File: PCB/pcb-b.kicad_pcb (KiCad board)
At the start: 2 copper layers, 117.6 x 56.4 mm, 90 parts, among them Q1 BC817, Q10 BC817, Q11 TPCA8120,L1Q, Q12 BC817, Q13 TPCA8120,L1Q, Q14 BC817, Q15 BC817, Q17 BC327, Q18 BC327, Q19 BC817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

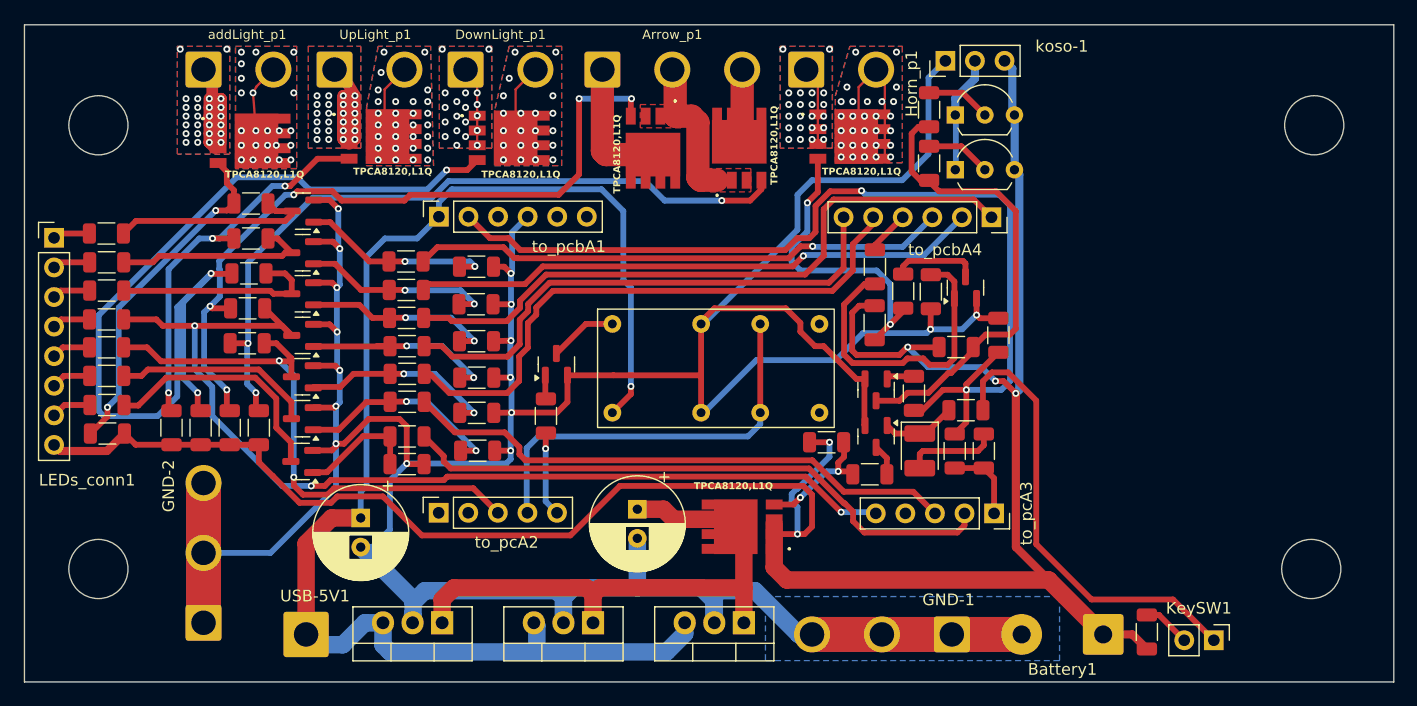
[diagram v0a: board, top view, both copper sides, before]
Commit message: Mechanic relay substitution and size reducing
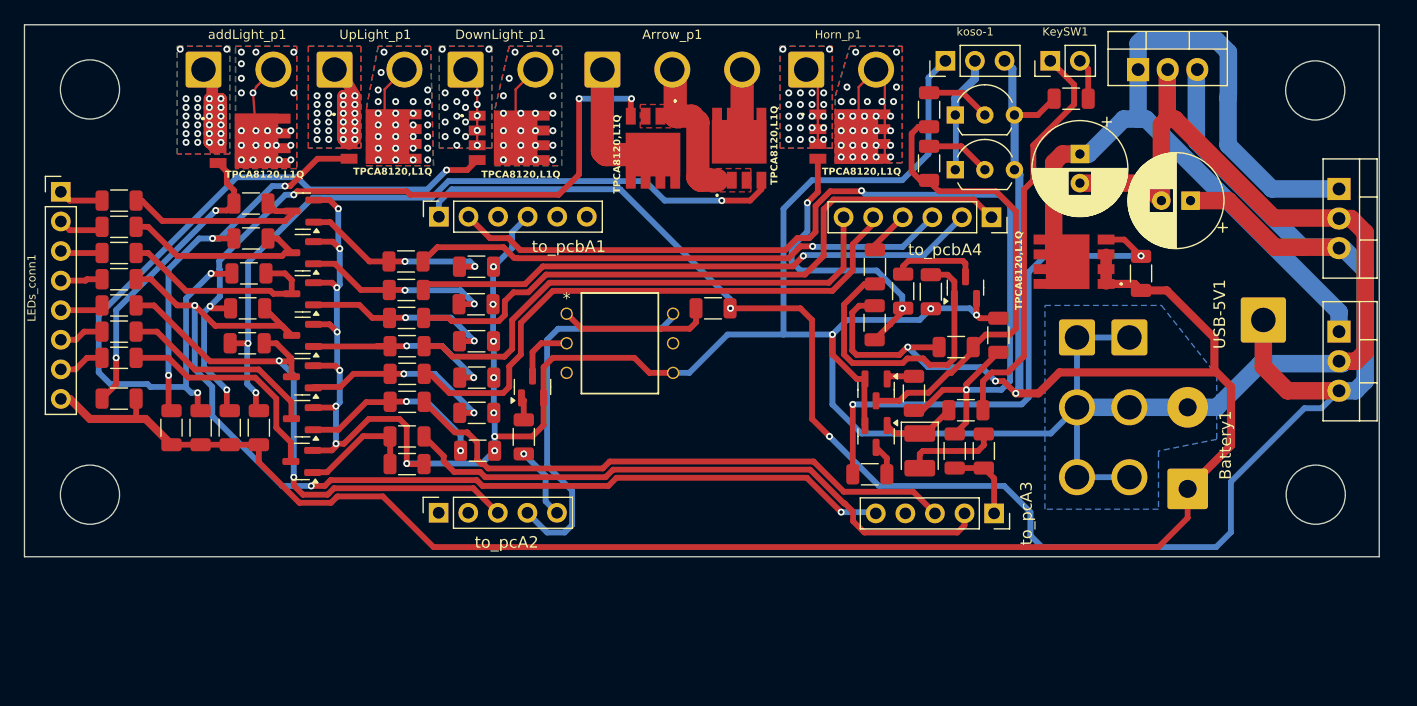
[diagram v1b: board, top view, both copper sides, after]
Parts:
- removed U4: HK19F-DC12-SHG, HK19F:HK19F-DC12-SHG
- added RA23: 1K, Resistor_SMD:R_1206_3216Metric, F.Cu at (158.7, 94.6)
- added U5: LH1511BT, LH1511BT:DIP_1511BT_VIS, F.Cu at (146.1, 95.1)
- moved USB-5V1 86.5 mm to (205.9, 95.6)
- moved GND-2 78.9 mm to (189.9, 97.1), turned to -90 degrees
- moved U3 76.3 mm to (195.2, 74.1), turned to 0 degrees
- moved C1 76.3 mm to (199.7, 85.3), turned to 180 degrees
- moved U2 68.8 mm to (212.4, 96.6), turned to -90 degrees
- moved U1 63.2 mm to (212.4, 84.3), turned to -90 degrees
- moved KeySW1 51.7 mm to (187.7, 73.3), turned to 90 degrees
- moved C9 48.7 mm to (190.2, 81.3)
- moved R1 46.2 mm to (189.4, 76.6), turned to 180 degrees
- moved Q13 36.5 mm to (189.7, 90.6)
- moved R2 30.6 mm to (195.4, 91.6), turned to 90 degrees
- moved GND-1 29.7 mm to (194.4, 97.1), turned to -90 degrees
- moved Battery1 14.5 mm to (199.4, 110.1), turned to 90 degrees
- moved RA9 4.18 mm to (107.7, 98.8)
- moved LEDs_conn1 3.99 mm to (102.7, 84.6)
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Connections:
- RA44 pad 1: Net-(Q12-B) -> o_engineON
- RA44 pad 2: o_engineON -> Net-(Q12-B)
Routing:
- net GND: track 351.7 -> 302.9 mm, vias 16 -> 18
- net tempPower: track 123.6 -> 169.8 mm, vias 1 -> 2
- net Net-(Q13-G): track 10.8 -> 46.3 mm
- net Net-(Q13-D_1): track 48.8 -> 77.4 mm
- net Net-(Q5-G): track 81.7 -> 67.3 mm
- net Net-(RA23-Pad1): track 0.00 -> 13.1 mm
- net +12V: track 206.7 -> 212.8 mm, vias 5 -> 3
- net Net-(KeySW1-Pin_1): track 39.4 -> 34.9 mm
- net Net-(Q11-G): track 29.5 -> 26.1 mm
- net c_leftArrow: track 87.8 -> 90.2 mm
- net Net-(Q20-B): track 18.1 -> 16.2 mm
- net c_engineOFF: track 35.1 -> 33.5 mm
- net Net-(Q21-C): track 20.8 -> 19.4 mm
- net o_engineON: track 7.30 -> 6.24 mm
- net o_neutral: track 48.2 -> 49.2 mm
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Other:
- board size 117.6 x 56.4 mm -> 116.3 x 45.7 mm

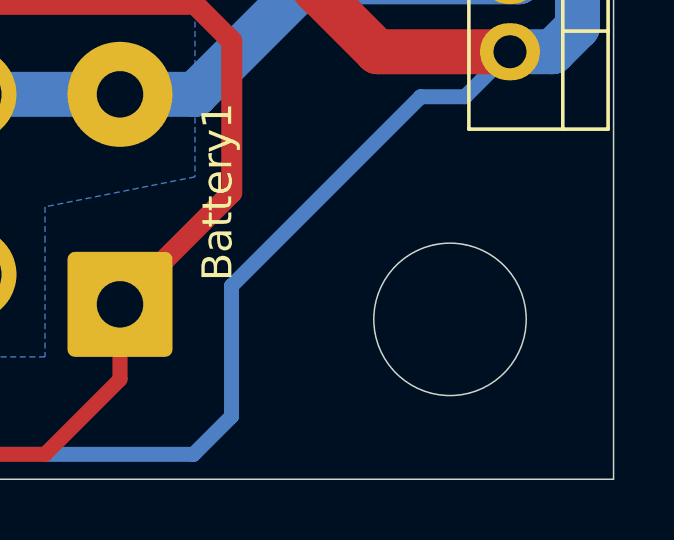
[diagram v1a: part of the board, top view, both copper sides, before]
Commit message: PCB's size reducing
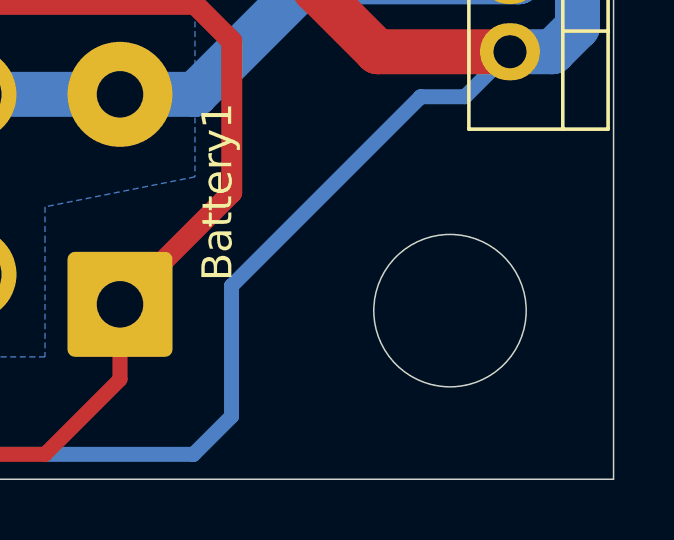
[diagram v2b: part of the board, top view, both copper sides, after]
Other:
- outline, holes or cut-outs redrawn
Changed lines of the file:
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@@
   (gr_circle (center 105.200067 75.806315) (end 107.740067 75.79575)
     (stroke (width 0.05) (type solid)) (fill none) (layer "Edge.Cuts"))
-  (gr_circle (center 210.450067 110.6) (end 212.990067 110.589435)
+  (gr_circle (center 210.45 110.309979) (end 212.99 110.299414)
     (stroke (width 0.05) (type solid)) (fill none) (layer "Edge.Cuts"))
   (gr_rect (start 99.576 70.255) (end 215.902 115.93)
@@
   (gr_circle (center 210.406315 75.890021) (end 215.036516 77.890021)
     (stroke (width 0.1) (type default)) (fill none) (layer "Margin"))
-  (gr_circle (center 210.45 110.6) (end 215.080201 112.6)
+  (gr_circle (center 210.449933 110.309979) (end 215.080134 112.309979)
     (stroke (width 0.1) (type default)) (fill none) (layer "Margin"))
   (dimension (type aligned) (layer "B.Mask")

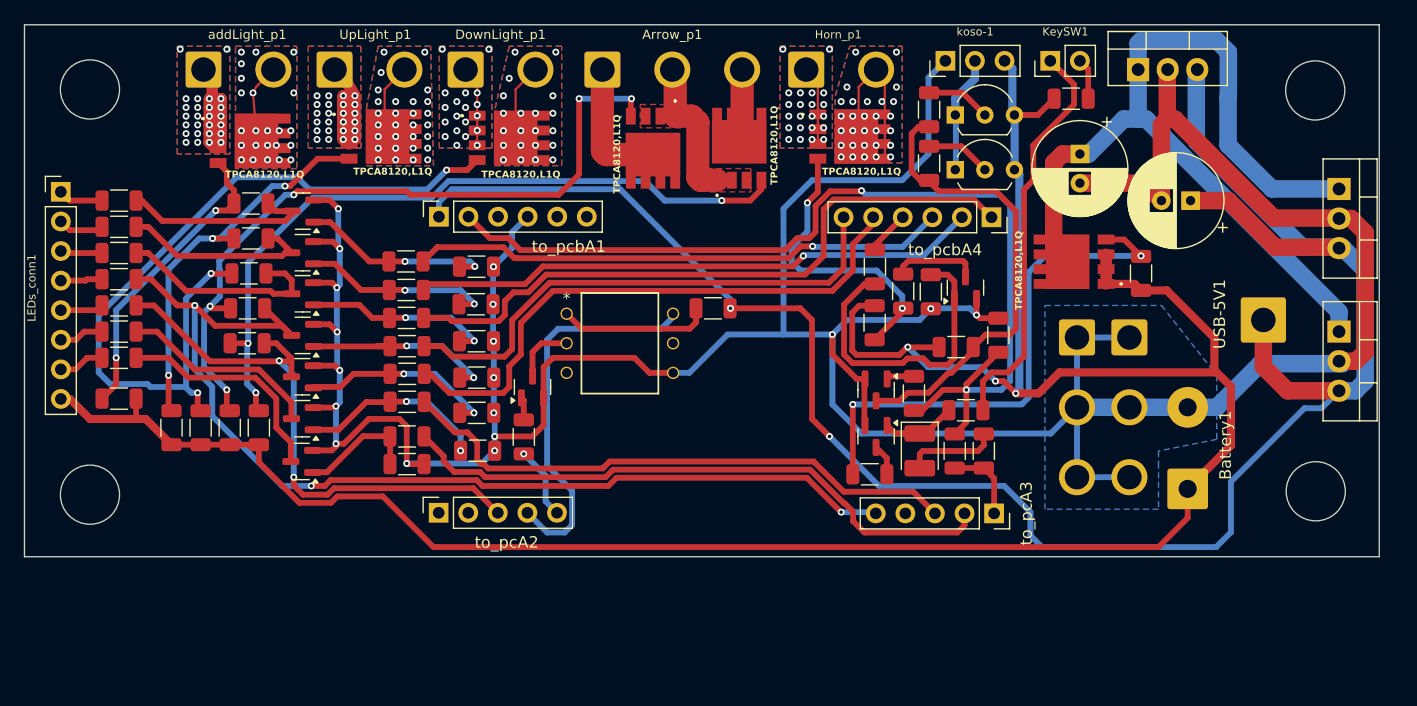
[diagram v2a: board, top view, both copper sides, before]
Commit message: Changes and enhancements
- File porting to Kicad-8
- Size reducing
- SSR has been replaced by Mosfet deplation N-Channel
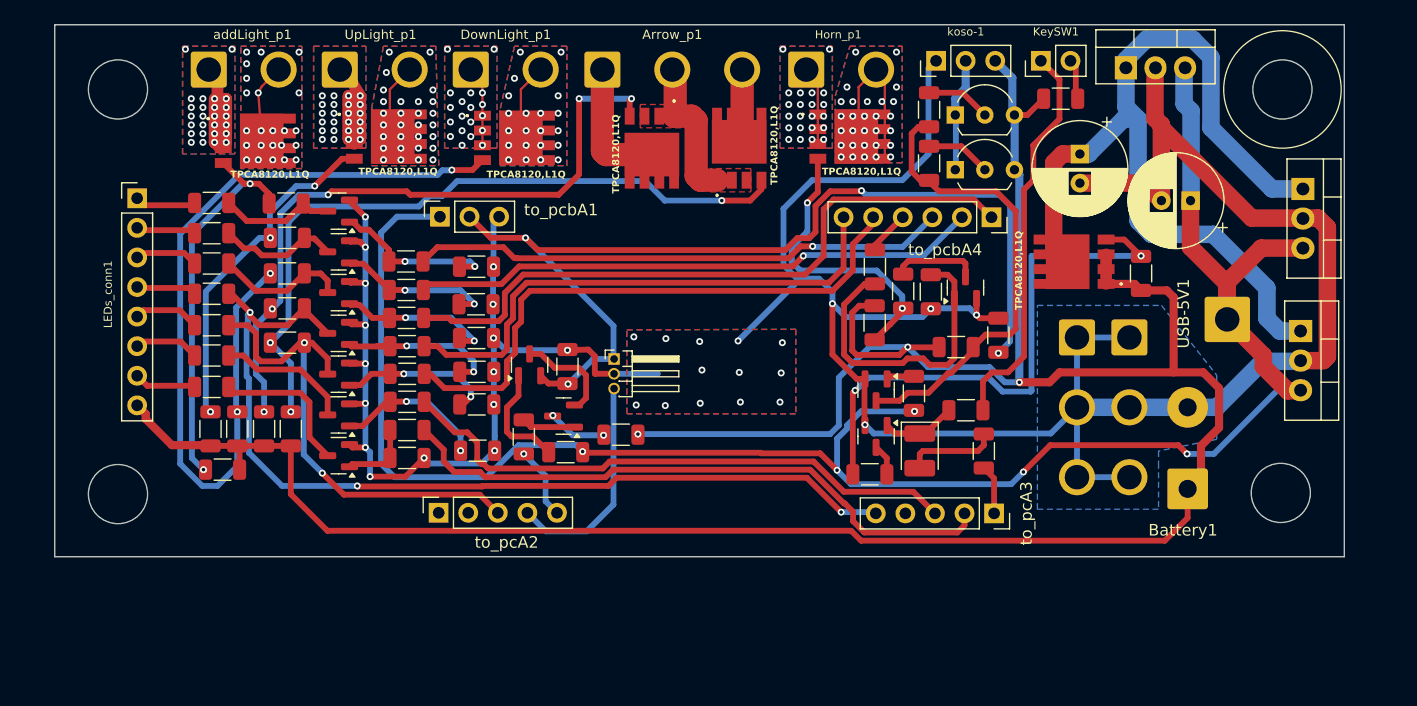
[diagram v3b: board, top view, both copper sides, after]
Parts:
- removed U5: LH1511BT, LH1511BT:DIP_1511BT_VIS
- added J1: IXTP3N50D2, Connector_PinHeader_1.27mm:PinHeader_1x03_P1.27mm_Horizontal, F.Cu at (150.2, 99.0)
- added Q16: BC817, Package_TO_SOT_SMD:SOT-23, F.Cu at (145.9, 103.8)
- added RA29: 3K, Resistor_SMD:R_1206_3216Metric, F.Cu at (146.2, 99.6)
- RA23: value 1K -> 10K
- RA43: value 10K -> 3K
- to_pcbA1: value Conn_01x06 -> Conn_01x03; footprint Connector_PinSocket_2.54mm:PinSocket_1x06_P2.54mm_Vertical -> Connector_PinSocket_2.54mm:PinSocket_1x03_P2.54mm_Vertical
- moved RA43 28.7 mm to (150.8, 105.5), turned to 180 degrees
- moved RA23 17.7 mm to (146.1, 107.0)
- moved RA24 10.8 mm to (116.6, 108.5)
- moved RA9 8.33 mm to (115.7, 101.3)
- moved RA6 8.21 mm to (115.7, 98.7)
- moved RA5 8.13 mm to (115.7, 96.0)
- moved RA4 8.05 mm to (115.7, 93.3)
- moved RA3 8.00 mm to (115.7, 90.8)
- moved RA2 7.97 mm to (115.7, 88.2)
- moved RA1 7.95 mm to (115.7, 85.5)
- moved LEDs_conn1 6.57 mm to (109.2, 85.2)
- moved RA14 3.45 mm to (122.2, 97.5)
- moved RA13 3.41 mm to (122.2, 94.6)
- moved RA25 3.35 mm to (115.5, 105.0)
- moved U2 3.30 mm to (209.2, 96.5)
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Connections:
- Q12 pad 2: GND -> i_powerOFF
- RA23 pad 1: Net-(RA23-Pad1) -> Net-(Q12-B)
- RA43 pad 1: i_powerOFF -> +12V
- RA43 pad 2: o_keepAlive -> Net-(Q16-C)
- RA44 pad 2: Net-(Q12-B) -> Net-(Q16-B)
- RA8 pad 1: i_powerOFF -> tempPower
- to_pcbA1 pad 3: unconnected-(to_pcbA1-Pin_3-Pad3) -> GND
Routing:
- net GND: track 302.9 -> 264.2 mm, vias 18 -> 33
- net +12V: track 212.8 -> 230.9 mm
- net c_engineOFF: track 33.5 -> 19.0 mm
- net Net-(RA23-Pad1): track 13.1 -> 0.00 mm
- net c_leftArrow: track 90.2 -> 80.2 mm
- net c_rightArrow: track 50.0 -> 41.9 mm
- net Net-(Q12-B): track 1.97 -> 9.54 mm
- net Net-(Q11-G): track 26.1 -> 33.3 mm
- net Net-(Q14-C): track 18.4 -> 11.4 mm
- net Net-(Q1-C): track 16.9 -> 10.0 mm
- net Net-(Q21-C): track 19.4 -> 12.7 mm
- net Net-(Q2-C): track 17.1 -> 10.4 mm
- net Net-(Q20-C): track 17.3 -> 11.5 mm
- net Net-(Q16-C): track 0.00 -> 5.05 mm, vias 0 -> 2
- net Net-(Q6-G): track 63.0 -> 58.0 mm
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- added copper zone on F.Cu, net GND
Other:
- board size 116.3 x 45.7 mm -> 110.7 x 45.7 mm

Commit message: Size reducing and component rationalization
- RS232(TTL) lines on PCB-B have been removed (MAX232 is already mounted in PCB-A)
- The two PCB can no more be connected using pin-header connectors. You have to use welded wires, now.
  (this solution is not beautiful as the original, but it is a more flexible one and it also allowd me
  to reduce the PCB size)

The PCBs size is approximately 109.7mm x 43.5mm.
For this dual-face sigle-layer (THT) version this is the minimum size I can achieve.
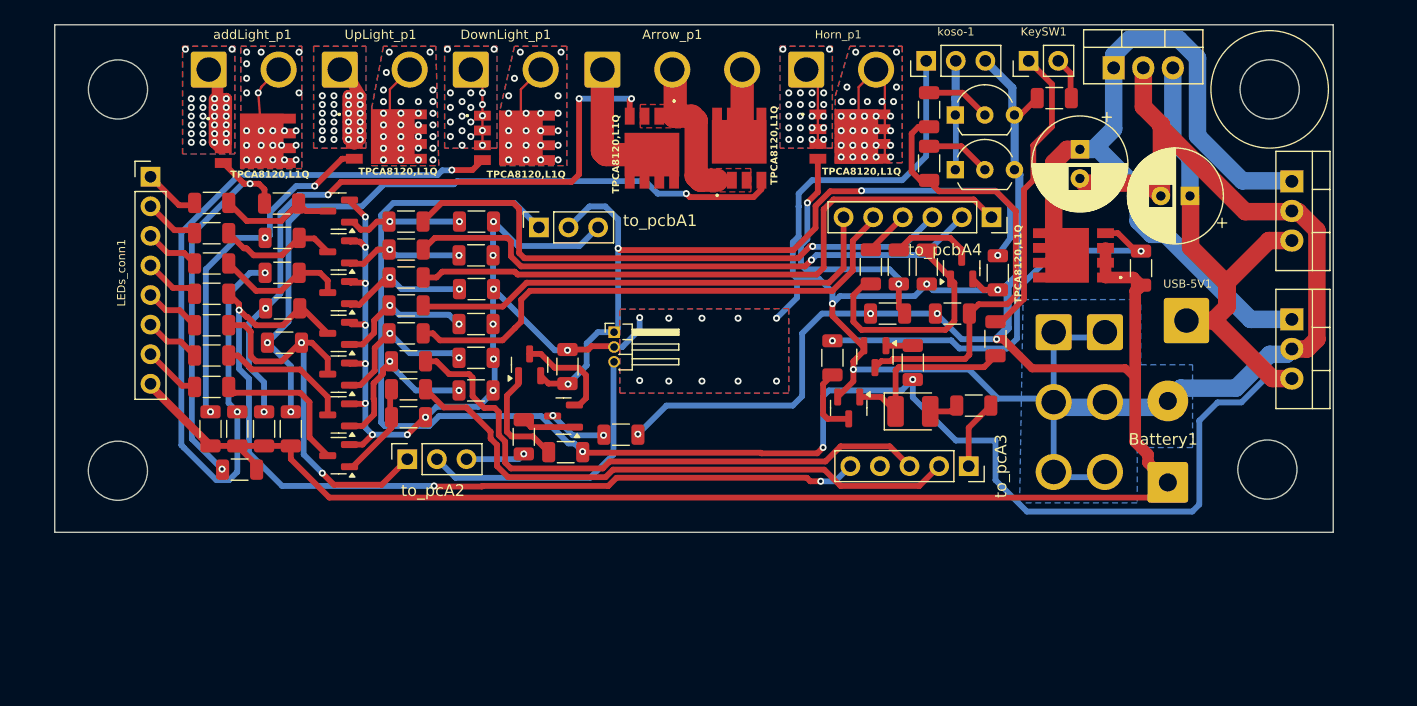
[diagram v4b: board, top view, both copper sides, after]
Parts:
- to_pcA2: value Conn_01x05 -> Conn_01x03; footprint Connector_PinSocket_2.54mm:PinSocket_1x05_P2.54mm_Vertical -> Connector_PinSocket_2.54mm:PinSocket_1x03_P2.54mm_Vertical
- moved R3 10.5 mm to (168.9, 98.8), turned to 90 degrees
- moved to_pcbA1 8.55 mm to (143.8, 87.7)
- moved R4 6.64 mm to (182.9, 97.2), turned to -90 degrees
- moved RA41 5.36 mm to (183.2, 91.5), turned to -90 degrees
- moved to_pcA2 5.33 mm to (132.4, 107.5)
- moved RA39 5.18 mm to (138.3, 101.7)
- moved to_pcA3 4.61 mm to (180.7, 108.2)
- moved RA35 4.20 mm to (138.3, 90.0)
- moved RA36 4.20 mm to (138.4, 93.0)
- moved RA37 4.10 mm to (138.3, 96.0)
- moved RA38 4.00 mm to (138.3, 98.8)
- moved R5 3.99 mm to (181.1, 103.0), turned to 0 degrees
- moved RA34 3.88 mm to (138.4, 87.2)
- moved RA16 3.50 mm to (132.6, 101.5)
- moved RA40 3.50 mm to (132.6, 104.0)
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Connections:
- to_pcA2 pad 1: c_RS232_RXD -> c_rightArrow
- to_pcA2 pad 2: c_RS232_TXT -> c_engineOFF
- to_pcA2 pad 3: c_rightArrow -> o_engineON
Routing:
- net +12V: track 230.9 -> 201.8 mm, vias 3 -> 4
- net i_powerOFF: track 86.3 -> 67.0 mm
- net tempPower: track 165.5 -> 180.9 mm, vias 5 -> 3
- net Net-(Q13-G): track 48.4 -> 36.4 mm
- net Net-(D1-K): track 6.41 -> 16.2 mm
- net Net-(KeySW1-Pin_1): track 34.2 -> 25.5 mm
- net c_rightArrow: track 41.9 -> 34.1 mm
- net Net-(Q3-B): track 26.9 -> 20.5 mm
- net c_engineOFF: track 19.0 -> 24.6 mm
- net Net-(D1-A): track 8.00 -> 2.48 mm
- net Net-(Q13-D_1): track 76.3 -> 71.8 mm
- net GND: track 264.2 -> 259.8 mm, vias 33 -> 30
- net Net-(Q1-B): track 14.4 -> 10.00 mm
- net o_leftArrow: track 46.2 -> 41.9 mm
- net o_addLight: track 46.1 -> 50.1 mm
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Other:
- board size 110.7 x 45.7 mm -> 109.8 x 43.6 mm
